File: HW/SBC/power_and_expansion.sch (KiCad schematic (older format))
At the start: 9 parts, among them J4 BARREL_JACK, J5 Expansion Port, U11 LM7805CT

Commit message: Moved IDE schematics (WIP) into pluto.
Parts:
- added MK5, MK6: Mounting_Hole, Mounting_Holes:MountingHole_3.2mm_M3_Pad, symbol Mounting_Hole
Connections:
- net labels removed: A0, A1, A10, A11, A12, A13, A14, A15, A2, A3, A4, A5, A6, A7, A8, A9, CLK, D0, D1, D2, D3, D4, D5, D6, D7, R/~W, ~7F0X, ~7F2X, ~7F4X, ~7F6X, ~7F8X, ~7FAX, ~IOSEL, ~IRQ, ~MRD, ~MWR, ~NMI, ~RES
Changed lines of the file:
@@
 EESchema Schematic File Version 2
+LIBS:pluto-rescue
 LIBS:power
 LIBS:device
@@
 $Descr A4 11693 8268
 encoding utf-8
-Sheet 6 7
+Sheet 6 8
 Title "Expansion port, power supply and decoupling capacitators"
 Date "2017-03-25"
@@
 	3850 6325 3850 6125
 Connection ~ 3600 6325
-Text GLabel 2925 4150 0    60   Input ~ 0
-A0
-Text GLabel 4250 4150 2    60   Input ~ 0
-A1
-Text GLabel 2925 4300 0    60   Input ~ 0
-A2
-Text GLabel 4250 4300 2    60   Input ~ 0
-A3
-Text GLabel 2925 4450 0    60   Input ~ 0
-A4
-Text GLabel 4250 4450 2    60   Input ~ 0
-A5
-Text GLabel 2925 4600 0    60   Input ~ 0
-A6
-Text GLabel 4250 4600 2    60   Input ~ 0
-A7
-Text GLabel 2925 4750 0    60   Input ~ 0
-A8
-Text GLabel 4250 4750 2    60   Input ~ 0
-A9
-Text GLabel 2925 4900 0    60   Input ~ 0
-A10
-Text GLabel 4250 4900 2    60   Input ~ 0
-A11
-Text GLabel 2925 5050 0    60   Input ~ 0
-A12
-Text GLabel 4250 5050 2    60   Input ~ 0
-A13
-Text GLabel 2925 5200 0    60   Input ~ 0
-A14
-Text GLabel 4250 5200 2    60   Input ~ 0
-A15
-Text GLabel 4250 5950 2    60   Input ~ 0
-~MWR
-Text GLabel 4250 6100 2    60   Input ~ 0
-~MRD
-Text GLabel 2925 5350 0    60   Input ~ 0
-~7F0X
-Text GLabel 4250 5350 2    60   Input ~ 0
-~7F2X
-Text GLabel 2925 5500 0    60   Input ~ 0
-~7F4X
-Text GLabel 4250 5500 2    60   Input ~ 0
-~7F6X
-Text GLabel 2925 5650 0    60   Input ~ 0
-~7F8X
-Text GLabel 2925 3550 0    60   Input ~ 0
-D0
-Text GLabel 4250 3550 2    60   Input ~ 0
-D1
-Text GLabel 2925 3700 0    60   Input ~ 0
-D2
-Text GLabel 4250 3700 2    60   Input ~ 0
-D3
-Text GLabel 2925 3850 0    60   Input ~ 0
-D4
-Text GLabel 4250 3850 2    60   Input ~ 0
-D5
-Text GLabel 2925 4000 0    60   Input ~ 0
-D6
-Text GLabel 4250 4000 2    60   Input ~ 0
-D7
-Text GLabel 2925 6250 0    60   Input ~ 0
-CLK
-Text GLabel 4250 6250 2    60   Input ~ 0
-~IRQ
-Text GLabel 2925 5950 0    60   Input ~ 0
-~IOSEL
-Text GLabel 2925 6100 0    60   Input ~ 0
-~NMI
-Text GLabel 2925 5800 0    60   Input ~ 0
-R/~W
-Text GLabel 4250 5800 2    60   Input ~ 0
-~RES
 Connection ~ 3225 2500
 $Comp
@@
 	1    0    0    -1
 $EndComp
-Text GLabel 4250 5650 2    60   Input ~ 0
-~7FAX
 $Comp
 L LM7805CT U11
@@
 Wire Wire Line
 	1350 1900 1350 2000
+$Comp
+L Mounting_Hole MK5
+U 1 1 5932DD04
+P 6050 4225
+F 0 "MK5" H 6050 4425 50  0000 C CNN
+F 1 "Mounting_Hole" H 6050 4350 50  0000 C CNN
+F 2 "Mounting_Holes:MountingHole_3.2mm_M3_Pad" H 6050 4225 50  0001 C CNN
+F 3 "" H 6050 4225 50  0001 C CNN
+	1    6050 4225
+	1    0    0    -1
+$EndComp
+$Comp
+L Mounting_Hole MK6
+U 1 1 5932DD62
+P 6750 4225
+F 0 "MK6" H 6750 4425 50  0000 C CNN
+F 1 "Mounting_Hole" H 6750 4350 50  0000 C CNN
+F 2 "Mounting_Holes:MountingHole_3.2mm_M3_Pad" H 6750 4225 50  0001 C CNN
+F 3 "" H 6750 4225 50  0001 C CNN
+	1    6750 4225
+	1    0    0    -1
+$EndComp
 $EndSCHEMATC

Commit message: Still no VCC net in PCBnew.
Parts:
- removed J5: Expansion Port, Connect:IDC_Header_Straight_50pins, symbol CONN_02X25
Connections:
- net labels removed: +9V
- wire segments 57 -> 13
- no-connect marks 8 -> 0
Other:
- moved on the sheet: C7, C8, MK1, MK2, MK3, MK4, MK5, MK6

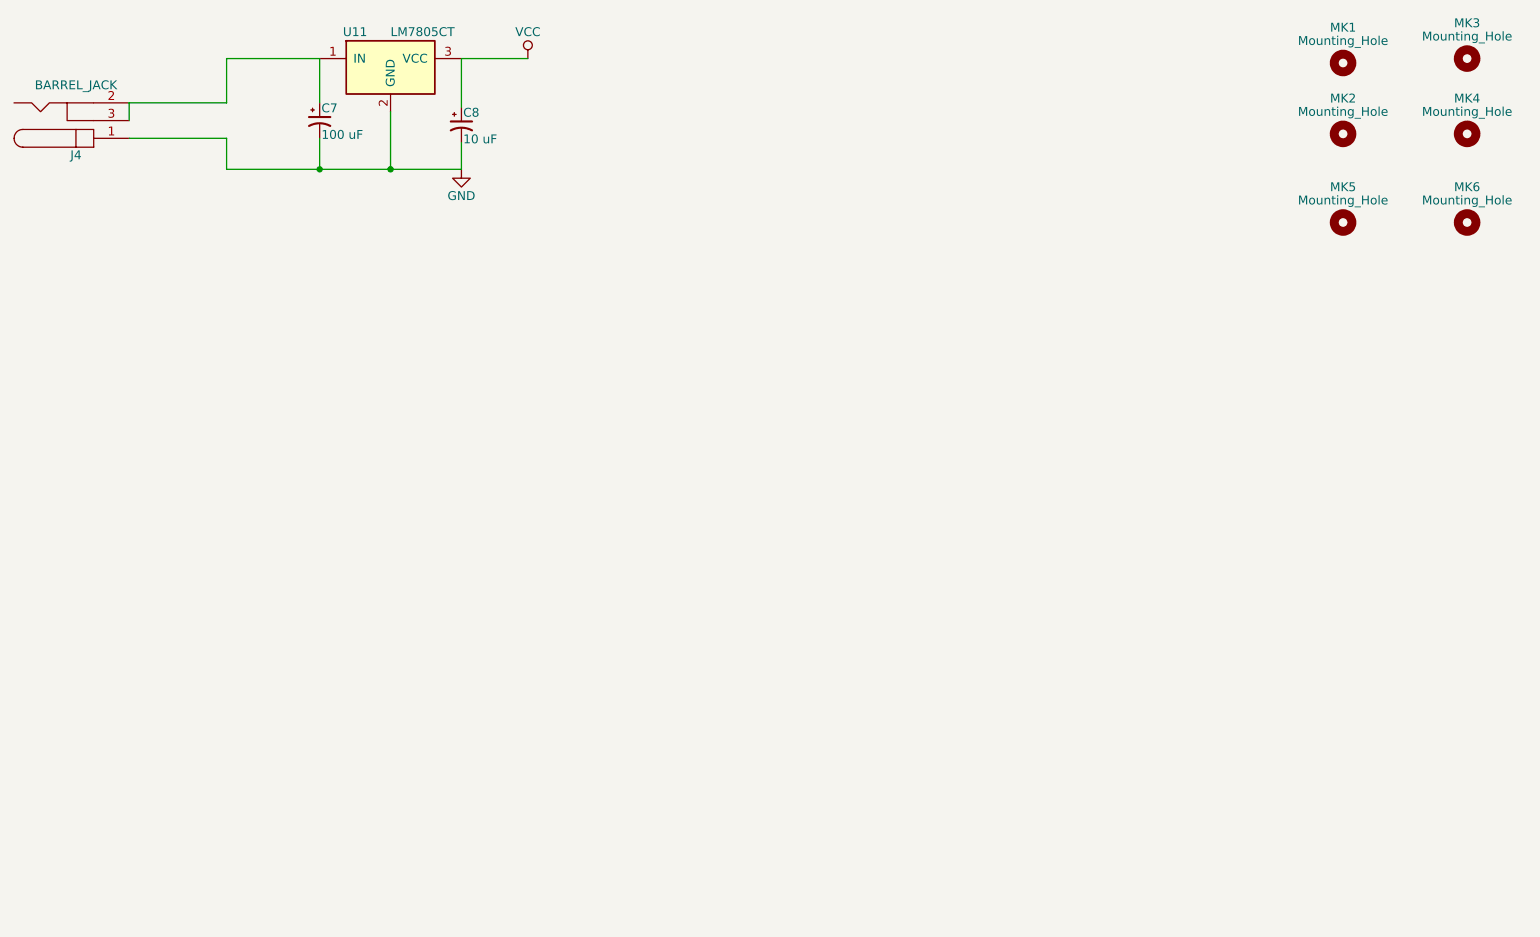
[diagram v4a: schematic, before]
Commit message: New PCB layout. Added datasheet for AY-3-8912 and LM386.
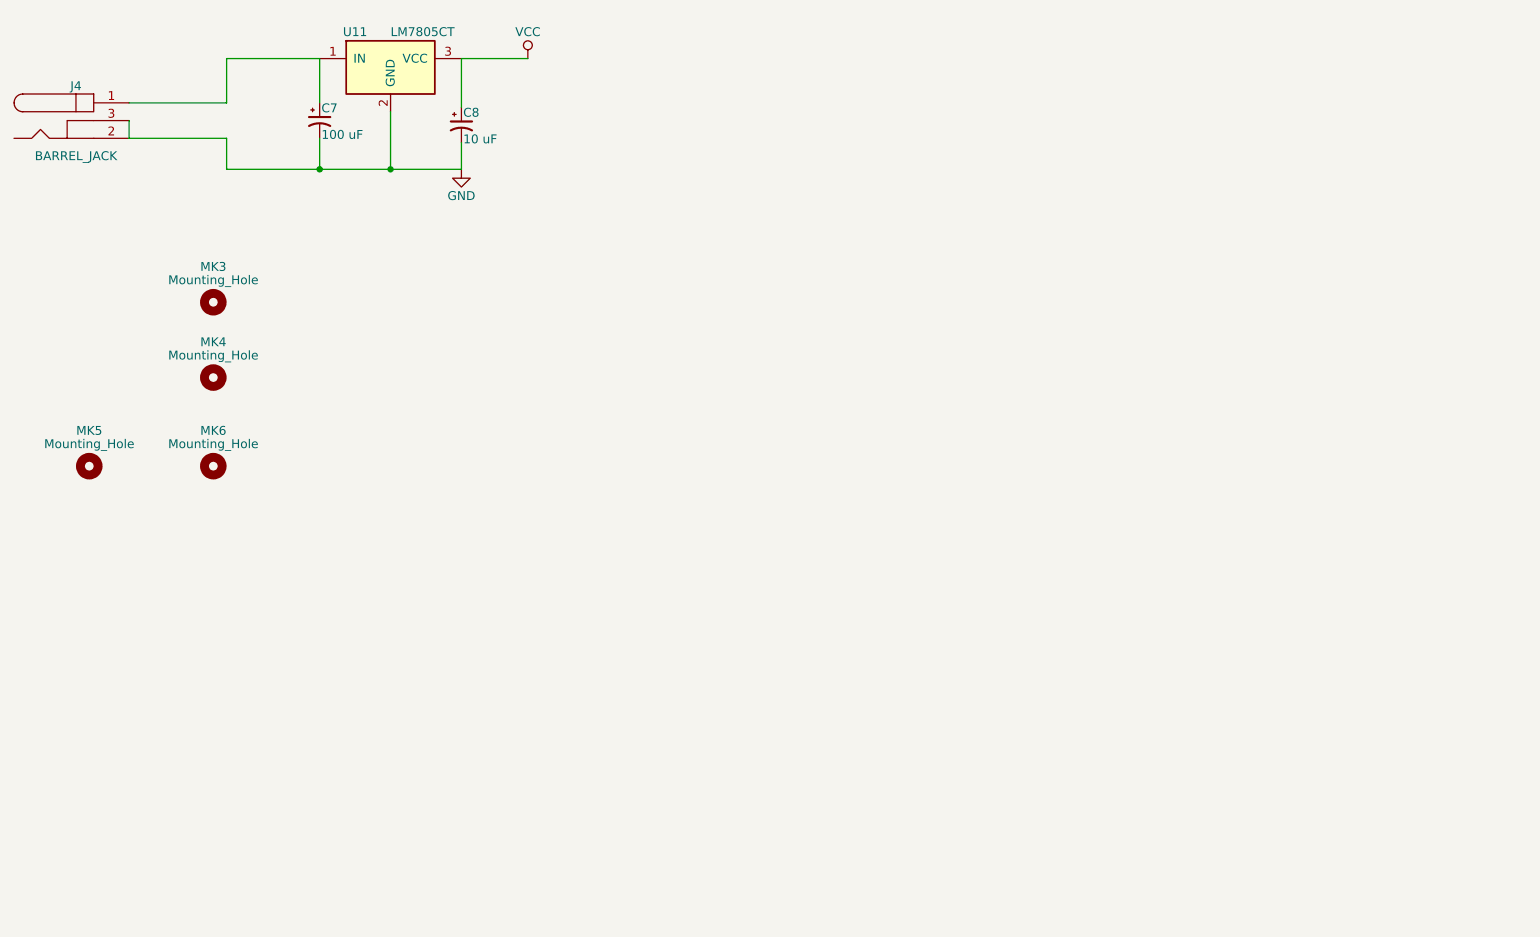
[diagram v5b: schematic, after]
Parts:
- removed MK1, MK2: Mounting_Hole, Mounting_Holes:MountingHole_3.2mm_M3_Pad, symbol Mounting_Hole
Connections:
- net GND: now also J4.2, J4.3; no longer J4.1
- net at C7.1, U11.1 (IN): now also J4.1; no longer J4.2, J4.3
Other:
- moved on the sheet: MK3, MK4, MK5, MK6
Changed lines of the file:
@@
 $EndDescr
-$Comp
-L Mounting_Hole MK1
-U 1 1 59149E0C
-P 8200 1675
-F 0 "MK1" H 8200 1875 50  0000 C CNN
-F 1 "Mounting_Hole" H 8200 1800 50  0000 C CNN
-F 2 "Mounting_Holes:MountingHole_3.2mm_M3_Pad" H 8200 1675 50  0001 C CNN
-F 3 "" H 8200 1675 50  0001 C CNN
-	1    8200 1675
-	1    0    0    -1
-$EndComp
-$Comp
-L Mounting_Hole MK2
-U 1 1 59149E41
-P 8200 2075
-F 0 "MK2" H 8200 2275 50  0000 C CNN
-F 1 "Mounting_Hole" H 8200 2200 50  0000 C CNN
-F 2 "Mounting_Holes:MountingHole_3.2mm_M3_Pad" H 8200 2075 50  0001 C CNN
-F 3 "" H 8200 2075 50  0001 C CNN
-	1    8200 2075
-	1    0    0    -1
-$EndComp
 $Comp
 L Mounting_Hole MK3
 U 1 1 59149E60
-P 8900 1650
-F 0 "MK3" H 8900 1850 50  0000 C CNN
-F 1 "Mounting_Hole" H 8900 1775 50  0000 C CNN
-F 2 "Mounting_Holes:MountingHole_3.2mm_M3_Pad" H 8900 1650 50  0001 C CNN
-F 3 "" H 8900 1650 50  0001 C CNN
-	1    8900 1650
+P 1825 3025
+F 0 "MK3" H 1825 3225 50  0000 C CNN
+F 1 "Mounting_Hole" H 1825 3150 50  0000 C CNN
+F 2 "Mounting_Holes:MountingHole_3.2mm_M3_Pad" H 1825 3025 50  0001 C CNN
+F 3 "" H 1825 3025 50  0001 C CNN
+	1    1825 3025
 	1    0    0    -1
 $EndComp
@@
 L Mounting_Hole MK4
 U 1 1 59149E83
-P 8900 2075
-F 0 "MK4" H 8900 2275 50  0000 C CNN
-F 1 "Mounting_Hole" H 8900 2200 50  0000 C CNN
-F 2 "Mounting_Holes:MountingHole_3.2mm_M3_Pad" H 8900 2075 50  0001 C CNN
-F 3 "" H 8900 2075 50  0001 C CNN
-	1    8900 2075
+P 1825 3450
+F 0 "MK4" H 1825 3650 50  0000 C CNN
+F 1 "Mounting_Hole" H 1825 3575 50  0000 C CNN
+F 2 "Mounting_Holes:MountingHole_3.2mm_M3_Pad" H 1825 3450 50  0001 C CNN
+F 3 "" H 1825 3450 50  0001 C CNN
+	1    1825 3450
 	1    0    0    -1
 $EndComp
@@
 L Mounting_Hole MK5
 U 1 1 5932DD04
-P 8200 2575
-F 0 "MK5" H 8200 2775 50  0000 C CNN
-F 1 "Mounting_Hole" H 8200 2700 50  0000 C CNN
-F 2 "Mounting_Holes:MountingHole_3.2mm_M3_Pad" H 8200 2575 50  0001 C CNN
-F 3 "" H 8200 2575 50  0001 C CNN
-	1    8200 2575
+P 1125 3950
+F 0 "MK5" H 1125 4150 50  0000 C CNN
+F 1 "Mounting_Hole" H 1125 4075 50  0000 C CNN
+F 2 "Mounting_Holes:MountingHole_3.2mm_M3_Pad" H 1125 3950 50  0001 C CNN
+F 3 "" H 1125 3950 50  0001 C CNN
+	1    1125 3950
 	1    0    0    -1
 $EndComp
@@
 L Mounting_Hole MK6
 U 1 1 5932DD62
-P 8900 2575
-F 0 "MK6" H 8900 2775 50  0000 C CNN
-F 1 "Mounting_Hole" H 8900 2700 50  0000 C CNN
-F 2 "Mounting_Holes:MountingHole_3.2mm_M3_Pad" H 8900 2575 50  0001 C CNN
-F 3 "" H 8900 2575 50  0001 C CNN
-	1    8900 2575
+P 1825 3950
+F 0 "MK6" H 1825 4150 50  0000 C CNN
+F 1 "Mounting_Hole" H 1825 4075 50  0000 C CNN
+F 2 "Mounting_Holes:MountingHole_3.2mm_M3_Pad" H 1825 3950 50  0001 C CNN
+F 3 "" H 1825 3950 50  0001 C CNN
+	1    1825 3950
 	1    0    0    -1
 $EndComp
@@
 F 3 "" H 1050 2000 50  0001 C CNN
 	1    1050 2000
-	1    0    0    1
+	1    0    0    -1
 $EndComp
 $Comp
@@
 Wire Wire Line
 	1900 2100 1900 2275
-Wire Wire Line
-	1350 1900 1350 2000
 Wire Wire Line
 	3225 1650 3600 1650
@@
 	1    0    0    -1
 $EndComp
+Wire Wire Line
+	1350 2000 1350 2100
 $EndSCHEMATC

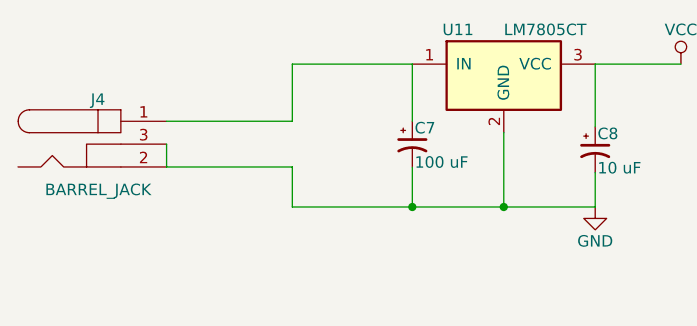
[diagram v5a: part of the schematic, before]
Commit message: Autorouted PCB.
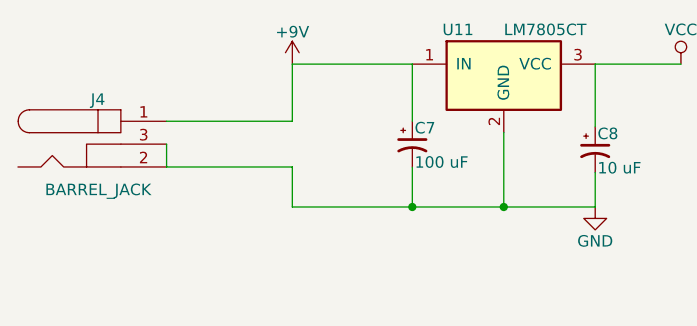
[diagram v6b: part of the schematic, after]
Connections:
- net +9V: now reaches C7.1, J4.1, U11.1 (IN)
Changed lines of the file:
@@
 Wire Wire Line
 	1350 2000 1350 2100
+$Comp
+L +9V #PWR?
+U 1 1 593AD94D
+P 1900 1650
+F 0 "#PWR?" H 1900 1500 50  0001 C CNN
+F 1 "+9V" H 1900 1790 50  0000 C CNN
+F 2 "" H 1900 1650 50  0001 C CNN
+F 3 "" H 1900 1650 50  0001 C CNN
+	1    1900 1650
+	1    0    0    -1
+$EndComp
 $EndSCHEMATC

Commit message: Added path to 65xx library
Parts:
- U11: symbol LM7805CT -> LM7805CT-RESCUE-pluto
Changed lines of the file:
@@
 EESchema Schematic File Version 2
+LIBS:pluto-rescue
 LIBS:power
 LIBS:device
@@
 $EndComp
 $Comp
-L LM7805CT U11
+L LM7805CT-RESCUE-pluto U11
 U 1 1 58E10ED4
 P 2825 1700
